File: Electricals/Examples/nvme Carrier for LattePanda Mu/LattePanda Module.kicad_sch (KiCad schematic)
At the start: 23 parts, among them J1 Conn_01x03_Pin, J81 Conn_01x02_Pin, U80 W25Q128JVSIQ

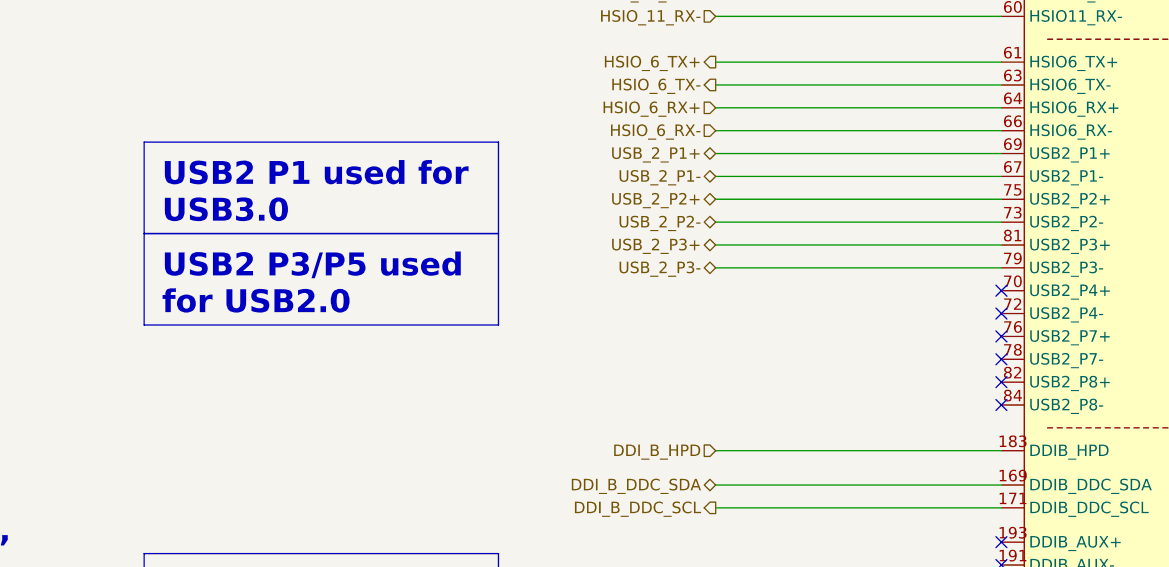
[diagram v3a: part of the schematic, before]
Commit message: Layout optimization + internal USB
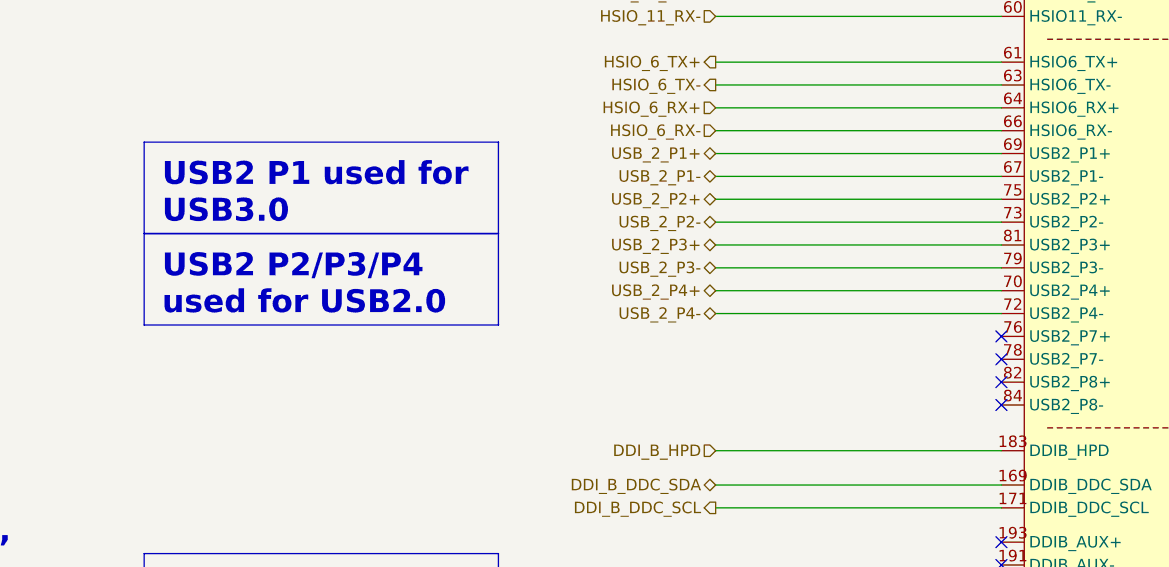
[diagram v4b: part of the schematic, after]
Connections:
- net USB_2_P4+: now reaches A1.70 (USB2_P4+)
- net USB_2_P4-: now reaches A1.72 (USB2_P4-)
- no-connect marks 96 -> 94
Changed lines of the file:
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@@
-	)
-	(no_connect
-		(at 270.51 190.5)
 	)
 	(no_connect
@@
 	)
 	(no_connect
-		(at 270.51 193.04)
-	)
-	(no_connect
 		(at 351.79 314.96)
 	)
@@
 	(wire
 		(pts
+			(xy 238.76 190.5) (xy 270.51 190.5)
+		)
+		(stroke
+			(width 0)
+			(type default)
+		)
+	)
+	(wire
+		(pts
 			(xy 463.55 228.6) (xy 471.17 228.6)
 		)
@@
 		(pts
 			(xy 238.76 132.08) (xy 270.51 132.08)
+		)
+		(stroke
+			(width 0)
+			(type default)
+		)
+	)
+	(wire
+		(pts
+			(xy 238.76 193.04) (xy 270.51 193.04)
 		)
 		(stroke
@@
 		)
 	)
-	(text_box "USB2 P3/P5 used for USB2.0 \n"
+	(text_box "USB2 P2/P3/P4 used for USB2.0 \n"
 		(exclude_from_sim no)
 		(at 175.26 184.15 0)
@@
 		)
 	)
+	(hierarchical_label "USB_2_P4-"
+		(shape bidirectional)
+		(at 238.76 193.04 180)
+		(fields_autoplaced yes)
+		(effects
+			(font
+				(size 1.27 1.27)
+			)
+			(justify right)
+		)
+	)
 	(hierarchical_label "HSIO_0_TX+"
 		(shape output)
@@
 		)
 	)
+	(hierarchical_label "USB_2_P4+"
+		(shape bidirectional)
+		(at 238.76 190.5 180)
+		(fields_autoplaced yes)
+		(effects
+			(font
+				(size 1.27 1.27)
+			)
+			(justify right)
+		)
+	)
